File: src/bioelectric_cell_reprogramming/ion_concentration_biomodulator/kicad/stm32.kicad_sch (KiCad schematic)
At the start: 25 parts, among them U6 STM32F407VGTx

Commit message: fix: new co2 sensor
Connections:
- net USART2_TX: now reaches U6.86 (PD5)
- net USART2_RX: now reaches U6.87 (PD6)
- no-connect marks 62 -> 60
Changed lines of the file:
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@@
-	)
-	(no_connect
-		(at 133.35 130.81)
 	)
 	(no_connect
@@
 	)
 	(no_connect
-		(at 133.35 128.27)
-	)
-	(no_connect
 		(at 133.35 102.87)
 	)
@@
 	(wire
 		(pts
+			(xy 144.78 130.81) (xy 133.35 130.81)
+		)
+		(stroke
+			(width 0)
+			(type default)
+		)
+	)
+	(wire
+		(pts
 			(xy 134.62 158.75) (xy 133.35 158.75)
 		)
@@
 		(pts
 			(xy 246.38 49.53) (xy 240.03 49.53)
+		)
+		(stroke
+			(width 0)
+			(type default)
+		)
+	)
+	(wire
+		(pts
+			(xy 144.78 128.27) (xy 133.35 128.27)
 		)
 		(stroke
@@
 		)
 	)
+	(label "USART2_RX"
+		(at 144.78 130.81 180)
+		(fields_autoplaced yes)
+		(effects
+			(font
+				(size 1.27 1.27)
+			)
+			(justify right bottom)
+		)
+	)
 	(label "I2C_SCK"
 		(at 71.12 119.38 0)
@@
 		)
 	)
+	(label "USART2_TX"
+		(at 144.78 128.27 180)
+		(fields_autoplaced yes)
+		(effects
+			(font
+				(size 1.27 1.27)
+			)
+			(justify right bottom)
+		)
+	)
 	(label "SOL4"
 		(at 77.47 158.75 0)
@@
 		)
 	)
+	(hierarchical_label "USART2_RX"
+		(shape input)
+		(at 144.78 130.81 0)
+		(fields_autoplaced yes)
+		(effects
+			(font
+				(size 1.27 1.27)
+			)
+			(justify left)
+		)
+	)
 	(hierarchical_label "SOL2"
 		(shape input)
@@
 		)
 	)
+	(hierarchical_label "USART2_TX"
+		(shape input)
+		(at 144.78 128.27 0)
+		(fields_autoplaced yes)
+		(effects
+			(font
+				(size 1.27 1.27)
+			)
+			(justify left)
+		)
+	)

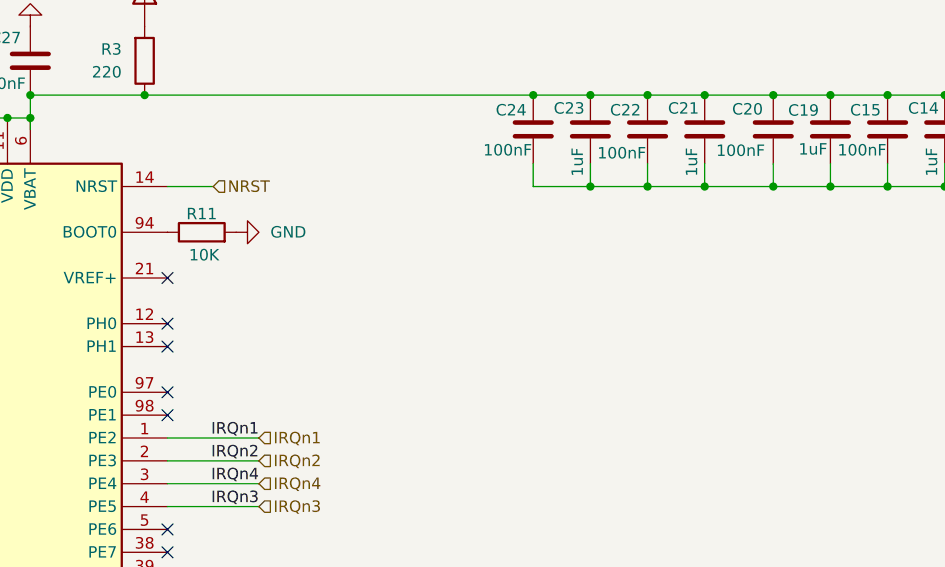
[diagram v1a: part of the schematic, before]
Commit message: fix: HSE for USB FS
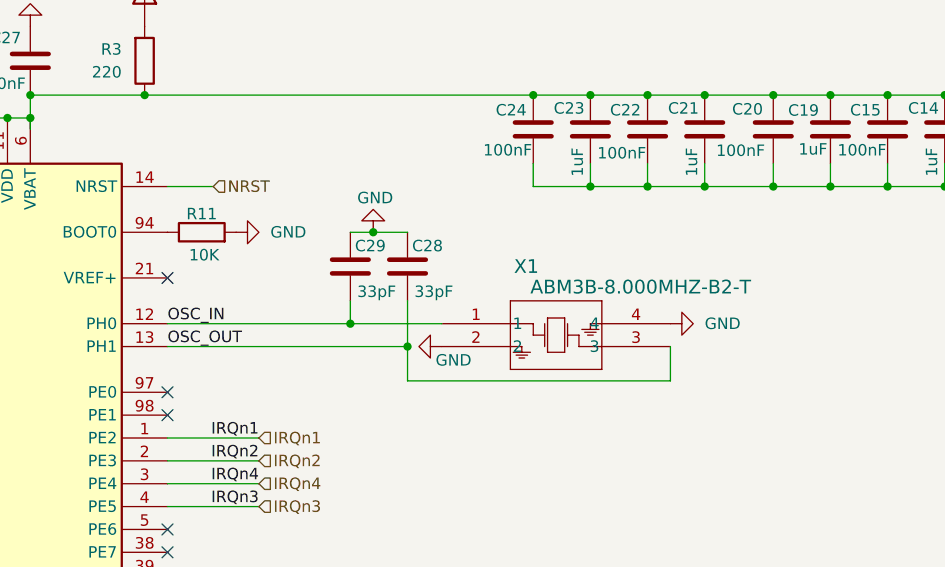
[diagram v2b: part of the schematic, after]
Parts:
- added C28, C29: 33pF, Capacitor_SMD:C_0201_0603Metric, symbol Device:C
- added X1: ABM3B-8.000MHZ-B2-T, ABM3B_8_000MHZ_B2_T:ABM3B_ABR, symbol ABM3B_8_000MHZ_B2_T:ABM3B-8.000MHZ-B2-T
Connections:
- net GND: now also C28.1, C29.1, X1.2, X1.4
- net OSC_IN: now reaches U6.12 (PH0)
- net OSC_IN: now also C29.2, X1.1
- net OSC_OUT: now reaches U6.13 (PH1)
- net OSC_OUT: now also C28.2, X1.3
- no-connect marks 60 -> 58
